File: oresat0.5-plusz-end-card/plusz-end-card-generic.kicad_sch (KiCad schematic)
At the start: 0 parts

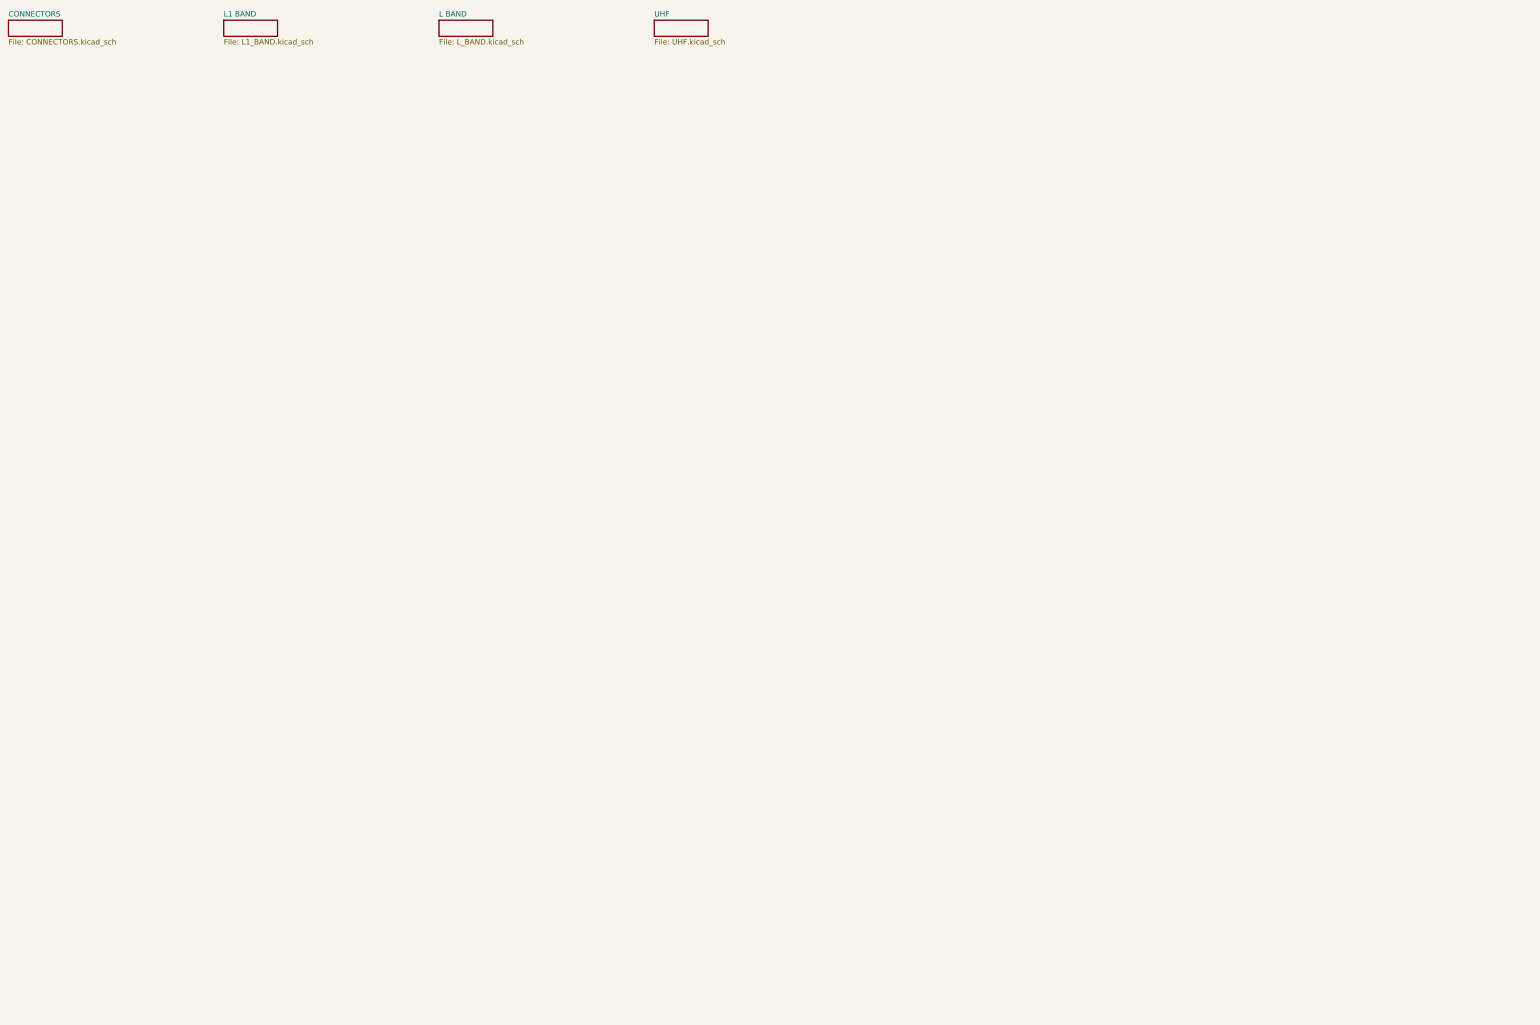
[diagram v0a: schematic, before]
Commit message: First rev of OreSat0.5 +Z end card. Updated helical deployer, removed as much EAGLE cruft as easily possible, killed multiple sch sheets.
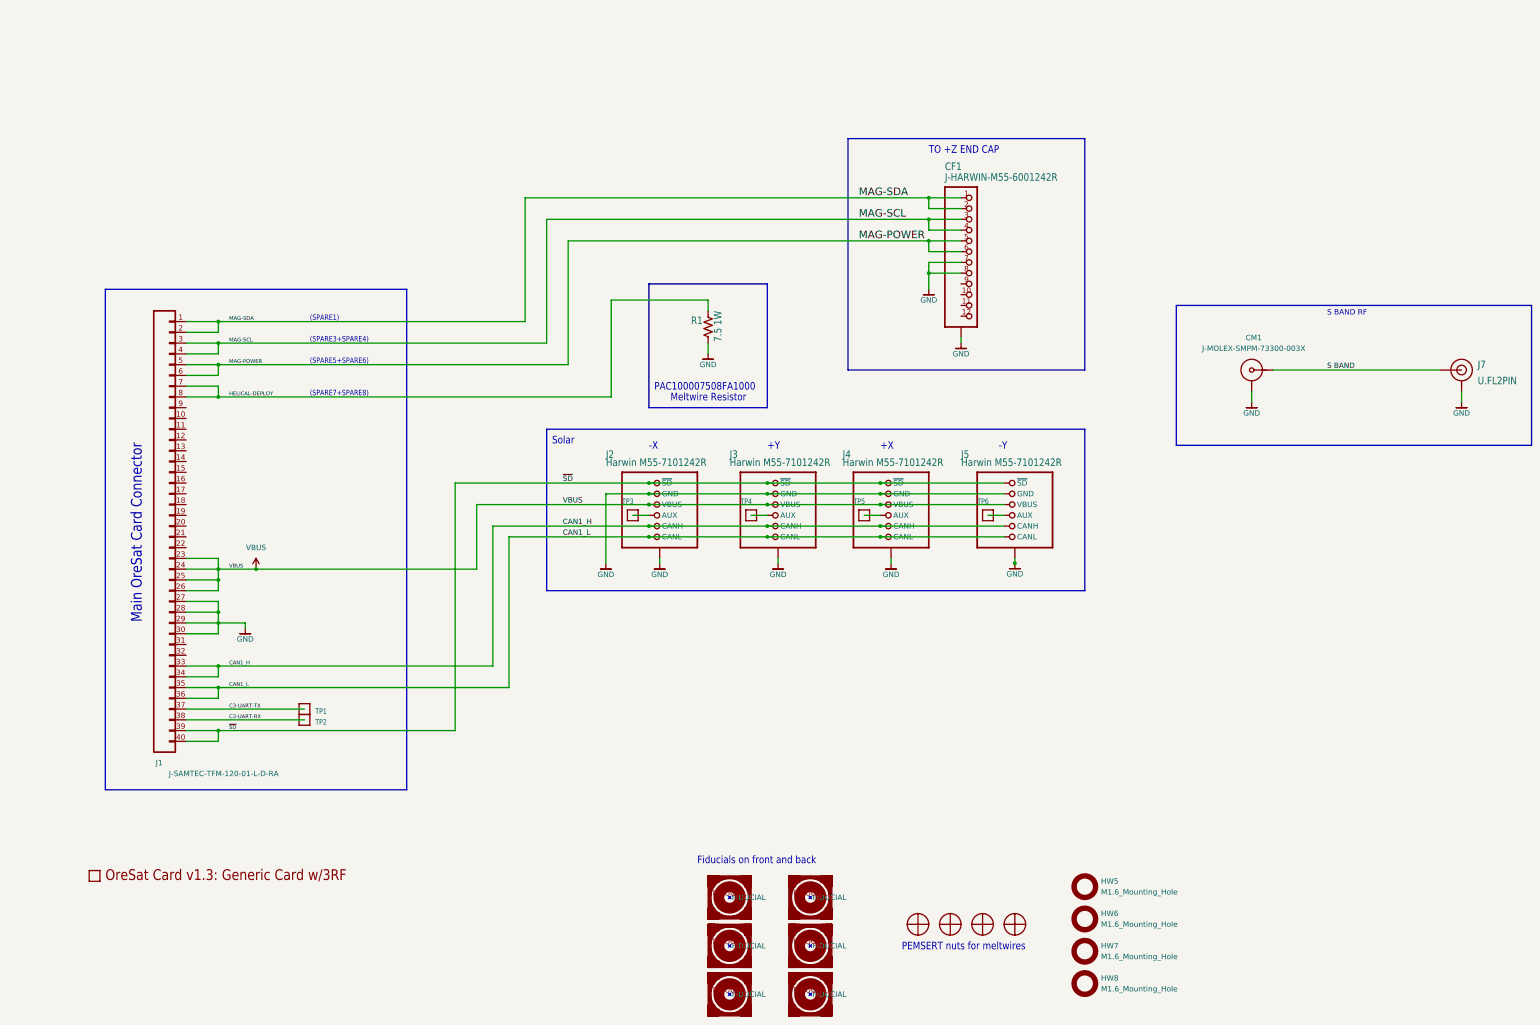
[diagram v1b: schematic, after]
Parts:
- added CF1: J-HARWIN-M55-6001242R, plusz-end-card-with-turnstile:HARWIN-M55-60X1242R, symbol plusz-end-card-with-turnstile-eagle-import:J-HARWIN-M55-60X1242R
- added CM1: J-MOLEX-SMPM-73300-003X, oresat-connectors:J-MOLEX-SMPM-073300-003X, symbol oresat-connectors:J-MOLEX-SMPM-73300-003X
- added FIDUCIAL1, FIDUCIAL2, FIDUCIAL3, FIDUCIAL4, FIDUCIAL5, FIDUCIAL6: FIDUCIAL-1.0X2.0, plusz-end-card-with-turnstile:FIDUCIAL-1.0X2.0, symbol plusz-end-card-with-turnstile-eagle-import:FIDUCIAL-1.0X2.0
- added HW1, HW2, HW3, HW4: MCMASTER-94100A150, oresat-footprints:H-MCMASTER-94100A150, symbol plusz-end-card-with-turnstile-eagle-import:MCMASTER-94100A150
- added HW5, HW6, HW7, HW8: M1.6_Mounting_Hole, oresat-misc:M1.6 Mounting Hole, symbol oresat-misc:M1.6_Mounting_Hole
- added J1: J-SAMTEC-TFM-120-01-L-D-RA, oresat-connectors:J-SAMTEC-TFM-120-X1-XXX-D-RA, symbol oresat-connectors:J-SAMTEC-TFM-120-01-L-D-RA
- added J2, J3, J4, J5: Harwin M55-7101242R, oresat-footprints:J-Harwin-M55-7101242R, symbol OreSat-j-solar-card-connector:SOLAR-CARD-CONNECTOR
- added J7: U.FL2PIN, oresat-connectors:U.FL_Molex_MCRF_73412-0110_Vertical, symbol oresat-connectors:U.FL2PIN
- added PCB1: ORESAT-CARD-V1.3-GENERIC-3RF, plusz-end-card-with-turnstile:ORESAT-CARD-V1.3-GENERIC-3RF, symbol plusz-end-card-with-turnstile-eagle-import:ORESAT-CARD-V1.3-GENERIC-3RF
- added R1: 7.5 1W, oresat-passives:R-PAC100-FOR-MELTWIRE, symbol Device:R_US
- added TP1, TP2, TP3, TP4, TP5, TP6: TEST-POINT-LARGE-SQUARE, plusz-end-card-with-turnstile:1X01, symbol plusz-end-card-with-turnstile-eagle-import:TEST-POINT-LARGE-SQUARE
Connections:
- new net: J4.7 (AUX), J4.8 (AUX), TP5.1
- new net: J2.7 (AUX), J2.8 (AUX), TP3.1
- new net: J5.7 (AUX), J5.8 (AUX), TP6.1
- new net: J3.7 (AUX), J3.8 (AUX), TP4.1
- new net C3-UART-RX: J1.38, TP2.1
- new net C3-UART-TX: J1.37, TP1.1
- new net CAN1_H: J1.33, J1.34, J2.10 (CANH), J2.9 (CANH), J3.10 (CANH), J3.9 (CANH), J4.10 (CANH), J4.9 (CANH), J5.10 (CANH), J5.9 (CANH)
- new net CAN1_L: J1.35, J1.36, J2.11 (CANL), J2.12 (CANL), J3.11 (CANL), J3.12 (CANL), J4.11 (CANL), J4.12 (CANL), J5.11 (CANL), J5.12 (CANL)
- new net GND: CF1.7, CF1.8, CF1.P$1 (SHIELDS), CF1.P$2 (SHIELDS), CF1.P$3 (SHIELDS), CF1.P$4 (SHIELDS), CM1.GND (SHIELD3), J1.27, J1.28, J1.29, J1.30, J2.3 (GND), J2.4 (GND), J2.GND (SHIELD), J3.3 (GND), J3.4 (GND), J3.GND (SHIELD), J4.3 (GND), J4.4 (GND), J4.GND (SHIELD), J5.3 (GND), J5.4 (GND), J5.GND (SHIELD), J7.GND, R1.1
- new net HELICAL-DEPLOY: J1.7, J1.8, R1.2
- new net MAG-POWER: CF1.5, CF1.6, J1.5, J1.6
- new net MAG-SCL: CF1.3, CF1.4, J1.3, J1.4
- new net MAG-SDA: CF1.1, CF1.2, J1.1, J1.2
- new net S BAND: CM1.RF (CENTER), J7.FEED (SIGNAL)
- new net VBUS: J1.23, J1.24, J1.25, J1.26, J2.5 (VBUS), J2.6 (VBUS), J3.5 (VBUS), J3.6 (VBUS), J4.5 (VBUS), J4.6 (VBUS), J5.5 (VBUS), J5.6 (VBUS)
- new net ~{SD}: J1.39, J1.40, J2.1 (~{SD}), J2.2 (~{SD}), J3.1 (~{SD}), J3.2 (~{SD}), J4.1 (~{SD}), J4.2 (~{SD}), J5.1 (~{SD}), J5.2 (~{SD})
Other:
- removed sheet CONNECTORS
- removed sheet L BAND
- removed sheet L1 BAND
- removed sheet UHF
- note added: "(SPARE1)"
- note added: "(SPARE3+SPARE4)"
- note added: "(SPARE5+SPARE6)"
- note added: "(SPARE7+SPARE8)"
- note added: "+X"
- note added: "+Y"
- note added: "-X"
- note added: "-Y"
- note added: "Fiducials on front and back"
- note added: "Main OreSat Card Connector"
- note added: "Meltwire Resistor"
- note added: "PAC100007508FA1000"
- note added: "PEMSERT nuts for meltwires"
- note added: "S BAND RF"
- note added: "Solar"
- note added: "TO +Z END CAP"

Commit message: More KiCADing, new fiducials and footprints, fixed ERC and DRC. Now waiting on Cesar to do stuff.
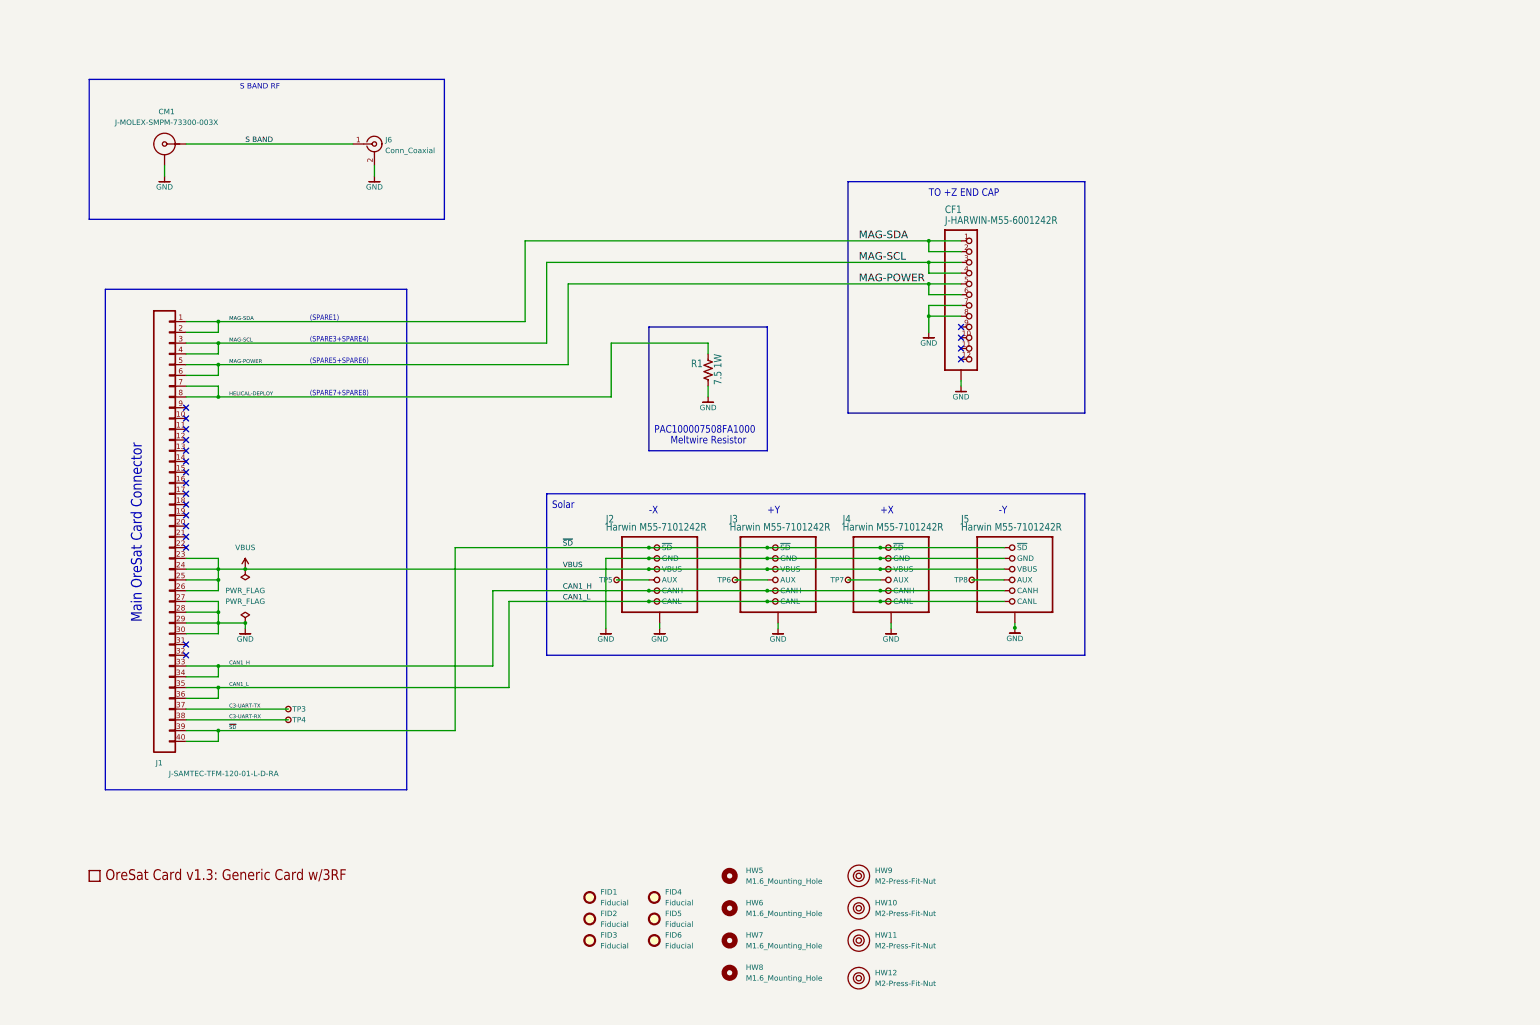
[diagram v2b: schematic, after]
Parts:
- removed FIDUCIAL1, FIDUCIAL2, FIDUCIAL3, FIDUCIAL4, FIDUCIAL5, FIDUCIAL6: FIDUCIAL-1.0X2.0, plusz-end-card-with-turnstile:FIDUCIAL-1.0X2.0, symbol plusz-end-card-with-turnstile-eagle-import:FIDUCIAL-1.0X2.0
- removed HW1, HW2, HW3, HW4: MCMASTER-94100A150, oresat-footprints:H-MCMASTER-94100A150, symbol plusz-end-card-with-turnstile-eagle-import:MCMASTER-94100A150
- removed J7: U.FL2PIN, oresat-connectors:U.FL_Molex_MCRF_73412-0110_Vertical, symbol oresat-connectors:U.FL2PIN
- removed TP1, TP2, TP3, TP4, TP5, TP6: TEST-POINT-LARGE-SQUARE, plusz-end-card-with-turnstile:1X01, symbol plusz-end-card-with-turnstile-eagle-import:TEST-POINT-LARGE-SQUARE
- added FID1, FID2, FID3, FID4, FID5, FID6: Fiducial, Fiducial:Fiducial_1mm_Mask2mm, symbol Mechanical:Fiducial
- added HW10, HW11, HW12, HW9: M2-Press-Fit-Nut, oresat-misc:M2-Press-Fit-Nut, symbol oresat-misc:M2-Press-Fit-Nut
- added J6: Conn_Coaxial, Connector_Coaxial:U.FL_Hirose_U.FL-R-SMT-1_Vertical, symbol Connector:Conn_Coaxial
- added TP3, TP4, TP5, TP6, TP7, TP8: TestPoint-MinTH, oresat-misc:TestPoint-MinTH, symbol oresat-misc:TestPoint-MinTH
- J1: footprint oresat-connectors:J-SAMTEC-TFM-120-X1-XXX-D-RA -> oresat-footprints:J-SAMTEC-TFM-120-X1-XXX-D-RA
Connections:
- net C3-UART-RX: now also TP4.1
- net C3-UART-TX: now also TP3.1
- net GND: now also J6.2 (Ext)
- net S BAND: now also J6.1 (In)
- net at J4.7 (AUX), J4.8 (AUX): now also TP7.1
- net at J2.7 (AUX), J2.8 (AUX): now also TP5.1
- net at J5.7 (AUX), J5.8 (AUX): now also TP8.1
- net at J3.7 (AUX), J3.8 (AUX): now also TP6.1
- no-connect marks 0 -> 20
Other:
- note removed: "Fiducials on front and back"
- note removed: "PEMSERT nuts for meltwires"
- moved on the sheet: CF1, CM1, HW5, HW6, HW7, HW8, J2, J3, J4, J5, R1
